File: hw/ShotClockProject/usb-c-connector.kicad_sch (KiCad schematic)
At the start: 4 parts, among them J1 USB4120-03-C_REVA, U6 USBLC6-2SC6

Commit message: Added I2C support
Calculated pull-up resistor values
Added 6 pin female headers to mainboard
Added nRESET line for the I2C chips
Removed PCB routing and part placement
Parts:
- renumbered J1 to J10
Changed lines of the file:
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@@
         )
         (path "/5fd859aa-754d-49c2-9762-3f7ebe3bb64c/946767ba-005d-422c-bf1d-949982eca775"
-          (reference "#FLG05") (unit 1)
+          (reference "#FLG011") (unit 1)
         )
       )
@@
         )
         (path "/5fd859aa-754d-49c2-9762-3f7ebe3bb64c/946767ba-005d-422c-bf1d-949982eca775"
-          (reference "R5") (unit 1)
+          (reference "R36") (unit 1)
         )
       )
@@
         )
         (path "/5fd859aa-754d-49c2-9762-3f7ebe3bb64c/946767ba-005d-422c-bf1d-949982eca775"
-          (reference "#FLG03") (unit 1)
+          (reference "#FLG010") (unit 1)
         )
       )
@@
         )
         (path "/5fd859aa-754d-49c2-9762-3f7ebe3bb64c/946767ba-005d-422c-bf1d-949982eca775"
-          (reference "#PWR03") (unit 1)
+          (reference "#PWR087") (unit 1)
         )
       )
@@
         )
         (path "/5fd859aa-754d-49c2-9762-3f7ebe3bb64c/946767ba-005d-422c-bf1d-949982eca775"
-          (reference "#PWR017") (unit 1)
+          (reference "#PWR091") (unit 1)
         )
       )
@@
         )
         (path "/5fd859aa-754d-49c2-9762-3f7ebe3bb64c/946767ba-005d-422c-bf1d-949982eca775"
-          (reference "#PWR086") (unit 1)
+          (reference "#PWR089") (unit 1)
         )
       )
@@
   (symbol (lib_id "USB4120-03-C_REVA:USB4120-03-C_REVA") (at 151.765 71.12 0) (unit 1)
     (in_bom yes) (on_board yes) (dnp no) (fields_autoplaced)
-    (property "Reference" "J1" (at 151.765 50.8 0)
+    (property "Reference" "J10" (at 151.765 50.8 0)
       (effects (font (size 1.27 1.27)))
     )
@@
       (project "ShotClockProject"
         (path "/5fd859aa-754d-49c2-9762-3f7ebe3bb64c/946767ba-005d-422c-bf1d-949982eca775"
-          (reference "J1") (unit 1)
+          (reference "J10") (unit 1)
         )
       )
@@
         )
         (path "/5fd859aa-754d-49c2-9762-3f7ebe3bb64c/946767ba-005d-422c-bf1d-949982eca775"
-          (reference "#PWR087") (unit 1)
+          (reference "#PWR090") (unit 1)
         )
       )
@@
         )
         (path "/5fd859aa-754d-49c2-9762-3f7ebe3bb64c/946767ba-005d-422c-bf1d-949982eca775"
-          (reference "#PWR011") (unit 1)
+          (reference "#PWR088") (unit 1)
         )
       )
@@
         )
         (path "/5fd859aa-754d-49c2-9762-3f7ebe3bb64c/946767ba-005d-422c-bf1d-949982eca775"
-          (reference "R7") (unit 1)
-        )
-      )
+          (reference "R37") (unit 1)
+        )
+      )

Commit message: Changed display connectors to JST PH 2.0mm
In docs, schematic and footprints
Both sides, connect with male/male cable
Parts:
- renumbered J10 to J6, U6 to U10
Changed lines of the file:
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@@
   (symbol (lib_id "Power_Protection:USBLC6-2SC6") (at 99.695 98.425 0) (unit 1)
     (in_bom yes) (on_board yes) (dnp no)
-    (property "Reference" "U6" (at 104.775 89.535 0)
+    (property "Reference" "U10" (at 104.775 89.535 0)
       (effects (font (size 1.27 1.27)) (justify left))
     )
@@
       (project "ShotClockProject"
         (path "/5fd859aa-754d-49c2-9762-3f7ebe3bb64c/946767ba-005d-422c-bf1d-949982eca775"
-          (reference "U6") (unit 1)
+          (reference "U10") (unit 1)
         )
       )
@@
   (symbol (lib_id "USB4120-03-C_REVA:USB4120-03-C_REVA") (at 151.765 71.12 0) (unit 1)
     (in_bom yes) (on_board yes) (dnp no) (fields_autoplaced)
-    (property "Reference" "J10" (at 151.765 50.8 0)
+    (property "Reference" "J6" (at 151.765 50.8 0)
       (effects (font (size 1.27 1.27)))
     )
@@
       (project "ShotClockProject"
         (path "/5fd859aa-754d-49c2-9762-3f7ebe3bb64c/946767ba-005d-422c-bf1d-949982eca775"
-          (reference "J10") (unit 1)
+          (reference "J6") (unit 1)
         )
       )

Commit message: Routed V regulators on mainboard
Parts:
- U10: now not fitted; now left out of the parts list
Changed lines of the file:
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@@
   )
   (symbol (lib_id "Power_Protection:USBLC6-2SC6") (at 99.695 98.425 0) (unit 1)
-    (in_bom yes) (on_board yes) (dnp no)
+    (in_bom no) (on_board no) (dnp yes)
     (property "Reference" "U10" (at 104.775 89.535 0)
       (effects (font (size 1.27 1.27)) (justify left))

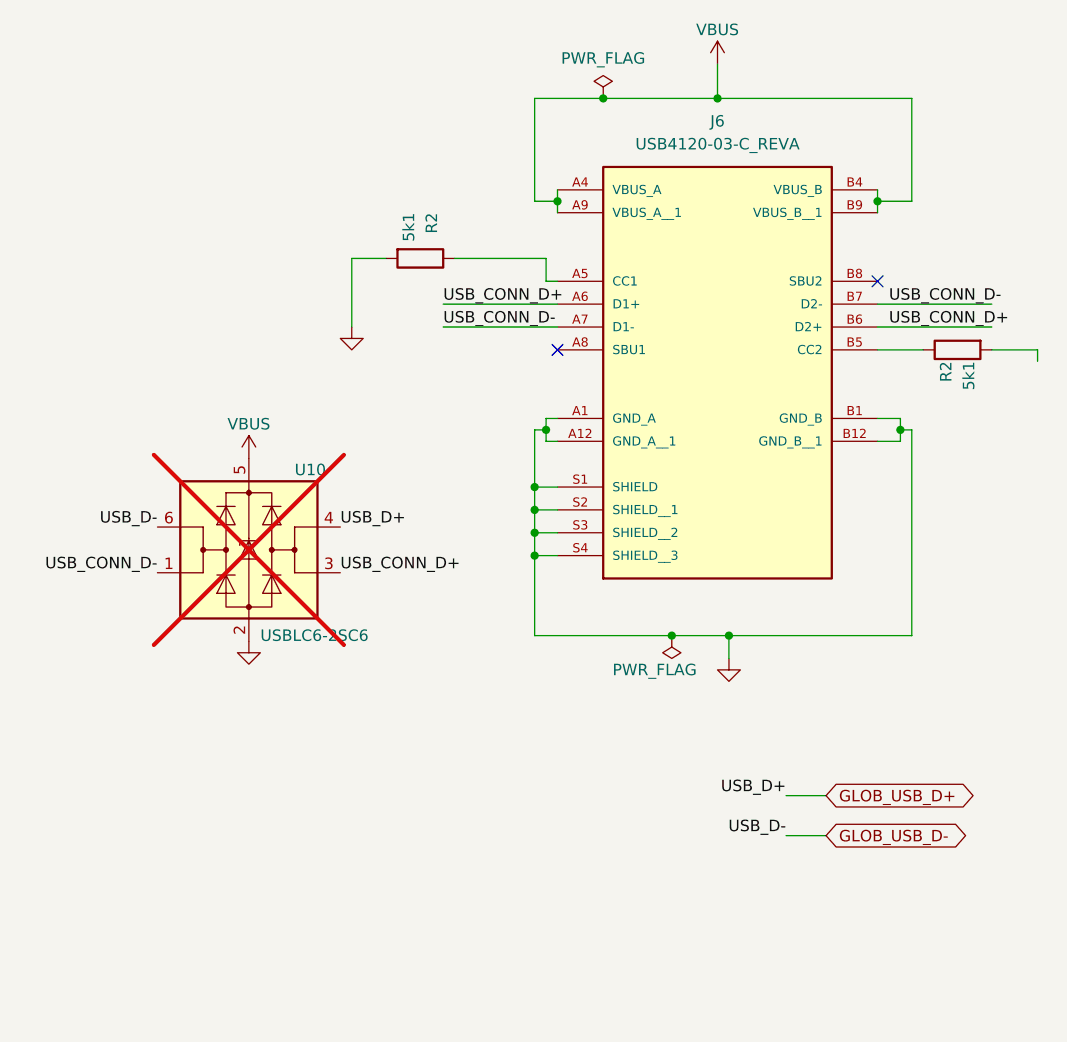
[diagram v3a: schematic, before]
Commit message: Routing on mainboard for LiPo charger
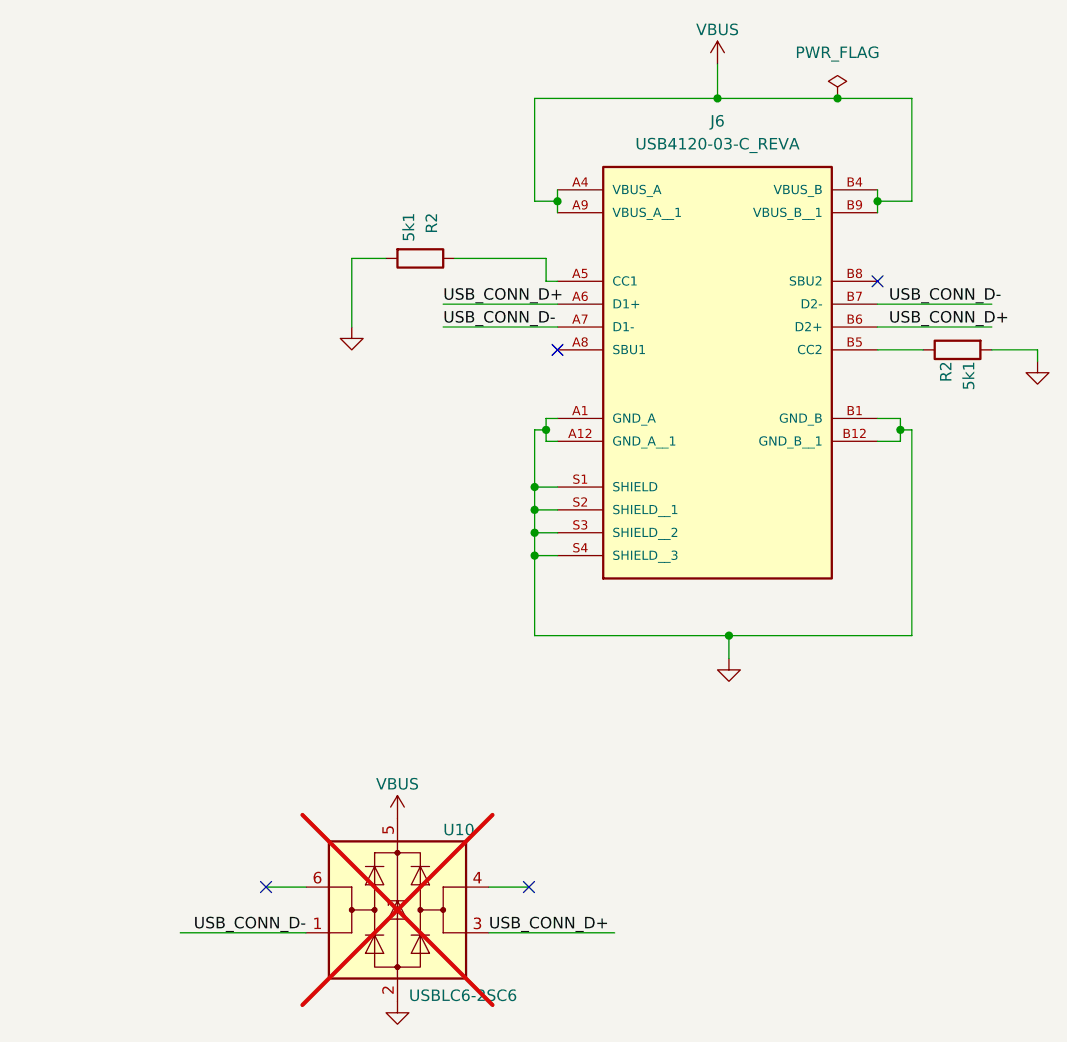
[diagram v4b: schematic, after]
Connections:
- net GND: now also R2.2
- net GLOB_USB_D+: no longer names the net of U10.4 (I/O2)
- net GLOB_USB_D-: no longer names the net of U10.6 (I/O1)
- no-connect marks 2 -> 4
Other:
- moved on the sheet: U10

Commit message: Finished mainboard routing
Reconfigered pins to make routing easier/cleaner
Placed copper fills as much as possible to create an even plating index
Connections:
- removed net USB_CONN_D+: J6.A6 (D1+), J6.B6 (D2+), U10.3 (I/O2)
- removed net USB_CONN_D-: J6.A7 (D1-), J6.B7 (D2-), U10.1 (I/O1)
- no-connect marks 4 -> 10
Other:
- note added: "USB_CONN_D+"
- note added: "USB_CONN_D-"
- note added: "USB_D+"
- note added: "USB_D-"
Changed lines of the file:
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@@
   )
   (no_connect (at 130.81 135.89))
+  (no_connect (at 133.985 73.66))
   (no_connect (at 101.6 135.89))
   (no_connect (at 133.985 76.2))
+  (no_connect (at 140.335 140.97))
+  (no_connect (at 169.545 73.66))
+  (no_connect (at 133.985 71.12))
+  (no_connect (at 92.075 140.97))
   (no_connect (at 169.545 68.58))
+  (no_connect (at 169.545 71.12))
   (wire (pts (xy 131.445 59.69) (xy 131.445 48.26))
     (stroke (width 0) (type default))
@@
   )
   (wire (pts (xy 126.365 140.97) (xy 140.335 140.97))
-    (stroke (width 0) (type default))
-  )
-  (wire (pts (xy 121.285 71.12) (xy 133.985 71.12))
     (stroke (width 0) (type default))
   )
@@
     (stroke (width 0) (type default))
   )
-  (wire (pts (xy 121.285 73.66) (xy 133.985 73.66))
-    (stroke (width 0) (type default))
-  )
   (wire (pts (xy 133.985 58.42) (xy 133.985 59.69))
     (stroke (width 0) (type default))
@@
   )
   (wire (pts (xy 92.075 140.97) (xy 106.045 140.97))
-    (stroke (width 0) (type default))
-  )
-  (wire (pts (xy 169.545 71.12) (xy 182.245 71.12))
     (stroke (width 0) (type default))
   )
@@
     (stroke (width 0) (type default))
   )
-  (wire (pts (xy 169.545 73.66) (xy 182.245 73.66))
-    (stroke (width 0) (type default))
-  )
   (wire (pts (xy 114.935 66.04) (xy 111.125 66.04))
     (stroke (width 0) (type default))
@@
     (stroke (width 0) (type default))
   )
-  (label "USB_CONN_D+" (at 170.815 73.66 0) (fields_autoplaced)
+  (text "USB_CONN_D-" (at 77.47 140.335 0)
     (effects (font (size 1.27 1.27)) (justify left bottom))
   )
-  (label "USB_CONN_D+" (at 126.365 140.97 0) (fields_autoplaced)
+  (text "USB_D-" (at 77.47 136.525 0)
     (effects (font (size 1.27 1.27)) (justify left bottom))
   )
-  (label "USB_CONN_D+" (at 121.285 71.12 0) (fields_autoplaced)
+  (text "USB_D+" (at 142.24 137.795 0)
     (effects (font (size 1.27 1.27)) (justify left bottom))
   )
-  (label "USB_CONN_D-" (at 121.285 73.66 0) (fields_autoplaced)
+  (text "USB_CONN_D+" (at 142.24 141.605 0)
     (effects (font (size 1.27 1.27)) (justify left bottom))
   )
-  (label "USB_CONN_D-" (at 170.815 71.12 0) (fields_autoplaced)
-    (effects (font (size 1.27 1.27)) (justify left bottom))
-  )
-  (label "USB_CONN_D-" (at 106.045 140.97 180) (fields_autoplaced)
-    (effects (font (size 1.27 1.27)) (justify right bottom))
-  )
   (symbol (lib_id "Device:R") (at 118.745 66.04 270) (unit 1)

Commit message: Finished routing and added silk + part nmbr
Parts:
- J6: LCSC Part # C5187468 -> (none)
- R2: LCSC Part # C25905 -> (none)
- U10: LCSC Part # C7519 -> (none)
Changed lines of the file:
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@@
       (effects (font (size 1.27 1.27)) hide)
     )
-    (property "LCSC Part #" "C25905" (at 118.745 66.04 0)
+    (property "LCSC Part #" "" (at 118.745 66.04 0)
       (effects (font (size 1.27 1.27)) hide)
     )
@@
       (effects (font (size 1.27 1.27)) hide)
     )
-    (property "LCSC Part #" "C7519" (at 116.205 138.43 0)
+    (property "LCSC Part #" "" (at 116.205 138.43 0)
       (effects (font (size 1.27 1.27)) hide)
     )
@@
       (effects (font (size 1.27 1.27)) (justify bottom) hide)
     )
-    (property "LCSC Part #" "C5187468" (at 151.765 71.12 0)
+    (property "LCSC Part #" "" (at 151.765 71.12 0)
       (effects (font (size 1.27 1.27)) hide)
     )
@@
       (effects (font (size 1.27 1.27)) hide)
     )
-    (property "LCSC Part #" "C25905" (at 178.435 76.2 0)
-      (effects (font (size 1.27 1.27)) hide)
-    )
+    (property "LCSC Part #" "" (at 178.435 76.2 0)
+      (effects (font (size 1.27 1.27)) hide)
+    )

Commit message: Add REV3 odt file, update CubeMX version and fix the ADC readout for battery voltage.
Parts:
- renumbered R2 to R36, R2 to R37
